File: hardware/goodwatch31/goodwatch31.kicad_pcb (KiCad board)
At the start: 2 copper layers, 25.6 x 27.6 mm, 23 parts, among them J1 ANT_U.FL, U1 CC430F613x, U2 0915LP15B02, U3 B0310J50100AHF, Y1 32.768kHz, Y2 FA128 26MHz

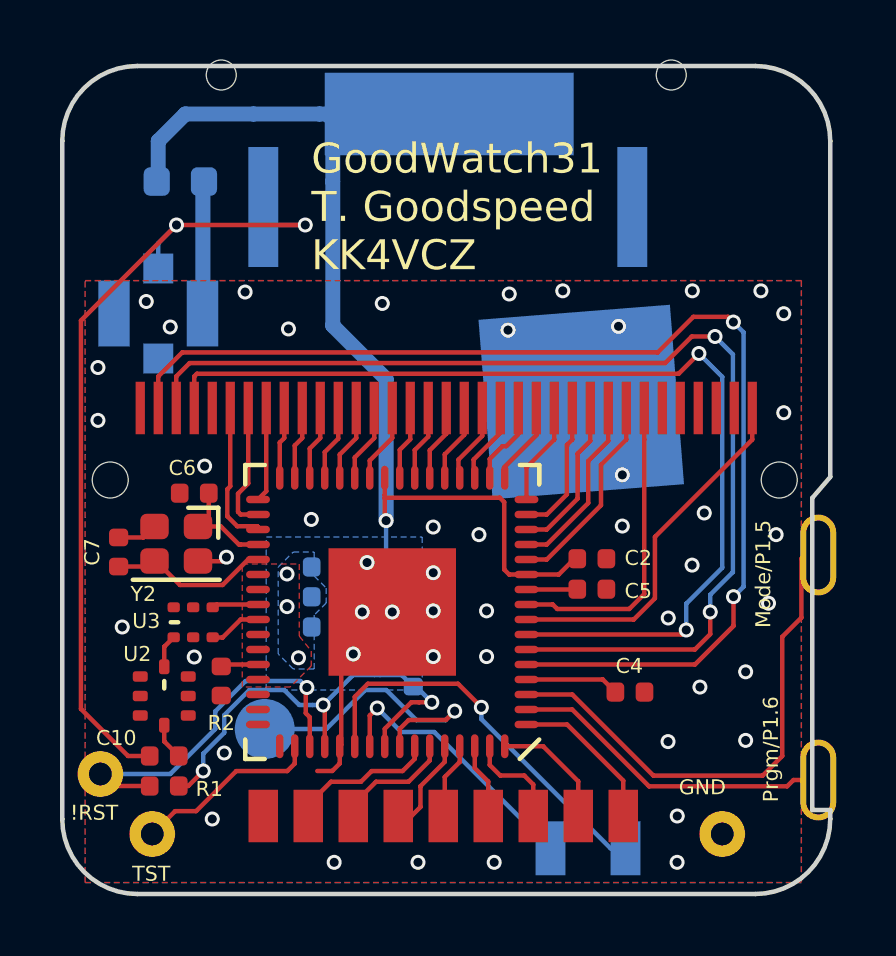
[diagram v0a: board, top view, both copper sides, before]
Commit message: Upgrade goodwatch31 files to KiCad 6 format
Also .gitignore
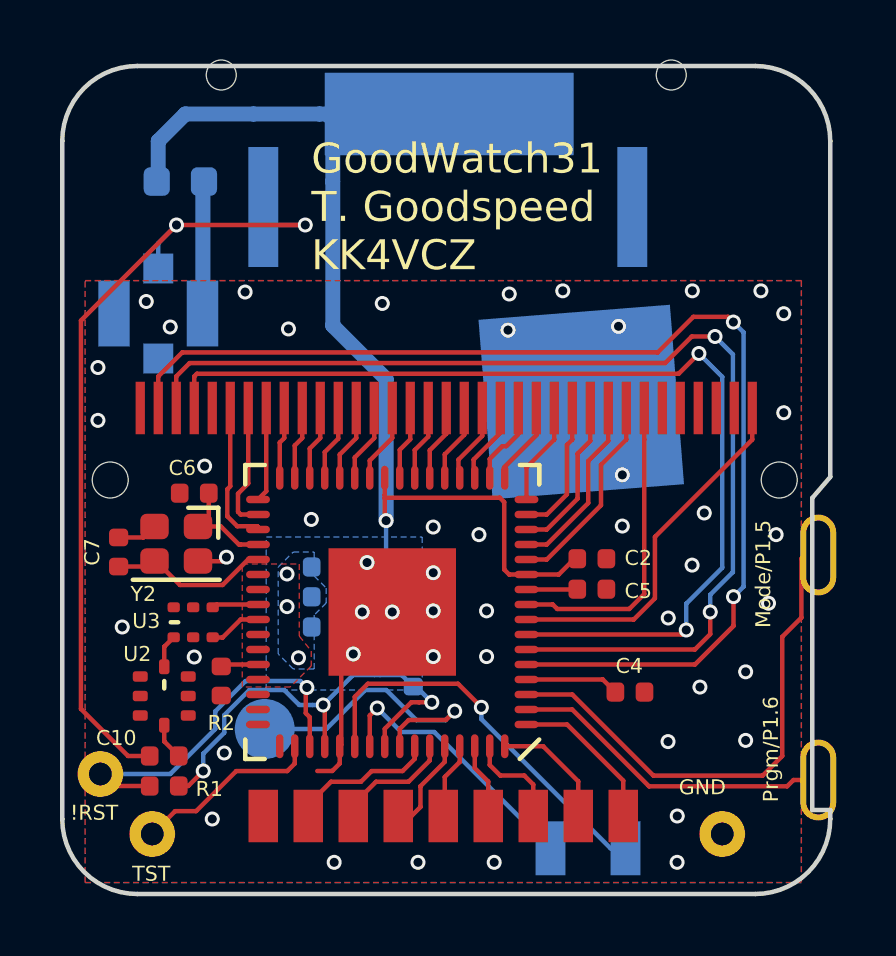
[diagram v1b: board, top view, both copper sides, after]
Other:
- net class Default removed
